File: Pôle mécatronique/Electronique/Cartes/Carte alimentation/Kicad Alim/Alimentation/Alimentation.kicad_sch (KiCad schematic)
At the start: 33 parts, among them J1 Conn_01x04, J10 24V in, J2 Conn_01x04, J3 Conn_01x04, J4 Conn_01x05, J5 Conn_01x05, J6 Conn_02x03_Odd_Even, J7 Conn_02x10_Odd_Even, J8 24V in, J9 24V out, K1 G5LE-1, Q1 BD135, SW1 SW_DPDT_x2, U1 TSR_2-2450, U2 TSR_2-2450, U3 TSR_2-24120

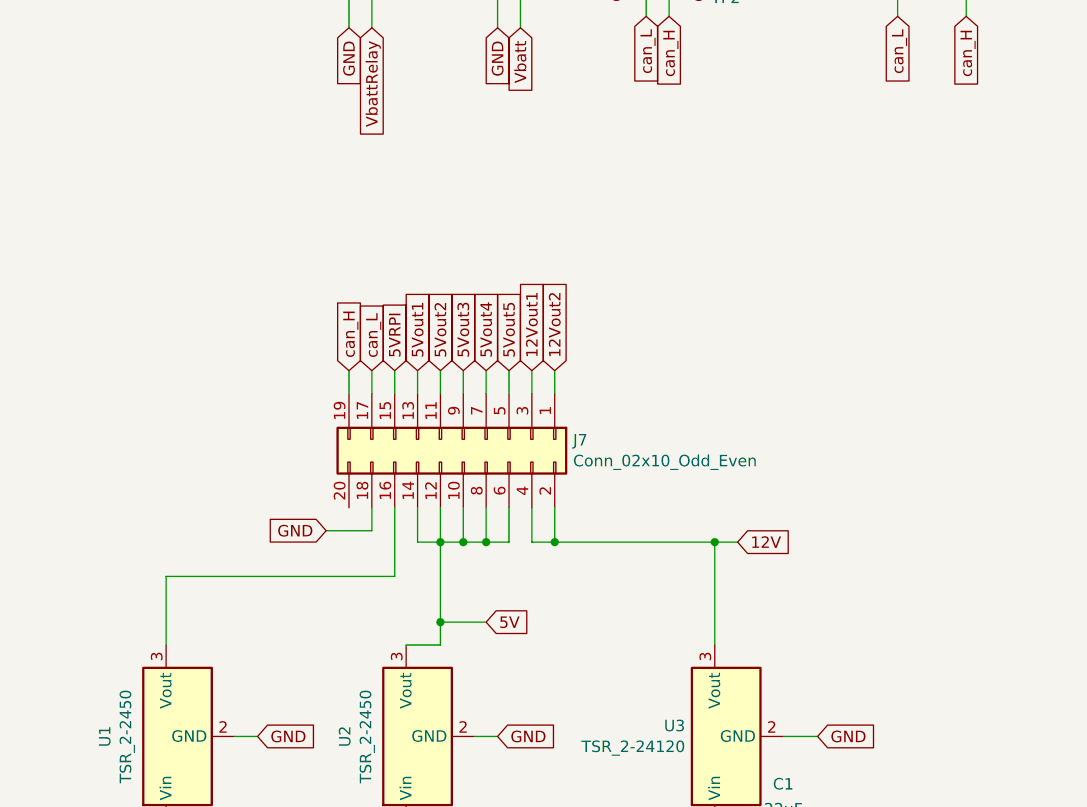
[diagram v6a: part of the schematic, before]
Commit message: Ajout points de masse
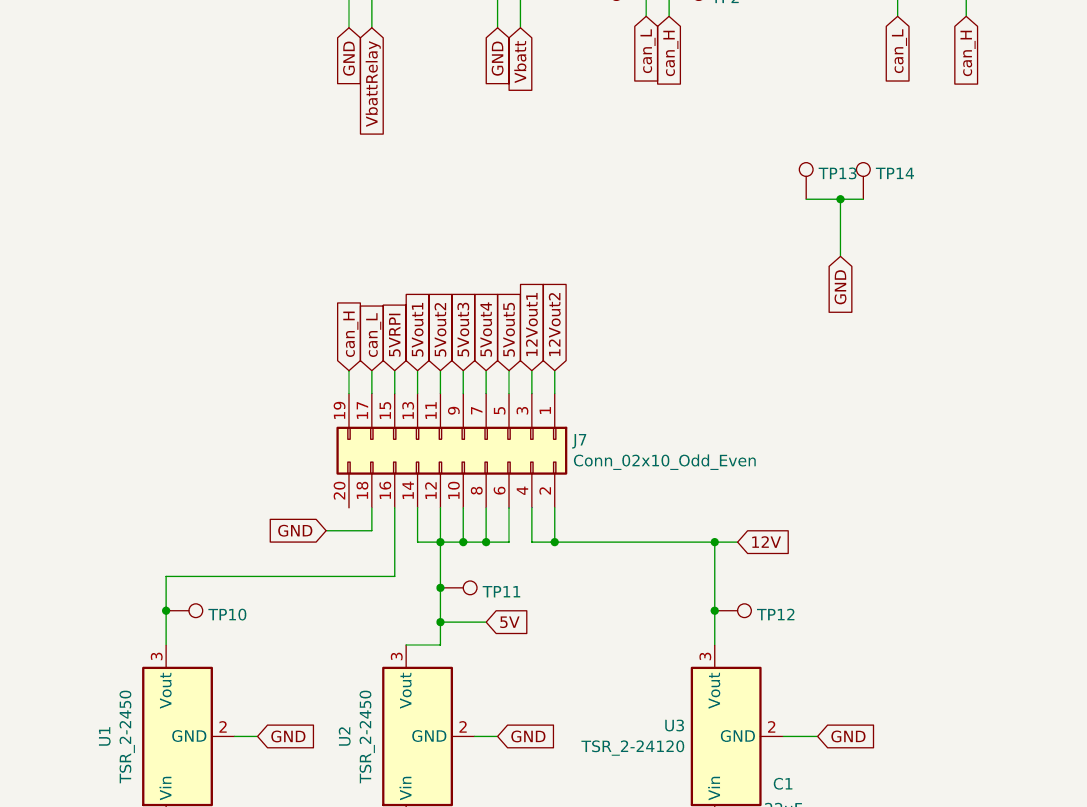
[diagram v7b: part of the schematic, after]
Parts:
- added TP10, TP11, TP12, TP13, TP14: TestPoint, TestPoint:TestPoint_Pad_D2.0mm, symbol Connector:TestPoint
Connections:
- net 12V: now also TP12.1
- net 5V: now also TP11.1
- net GND: now also TP13.1, TP14.1
- net at J7.16 (Pin_16), U1.3 (Vout): now also TP10.1
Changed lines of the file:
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@@
 (kicad_sch (version 20211123) (generator eeschema)
   (paper "A4")
+  (junction (at 63.5 140.97) (diameter 0) (color 0 0 0 0)
+  )
   (junction (at 152.4 71.12) (diameter 0) (color 0 0 0 0)
   )
@@
   (junction (at 99.06 133.35) (diameter 0) (color 0 0 0 0)
   )
+  (junction (at 138.43 95.25) (diameter 0) (color 0 0 0 0)
+  )
   (junction (at 232.41 78.74) (diameter 0) (color 0 0 0 0)
   )
@@
   (junction (at 96.52 133.35) (diameter 0) (color 0 0 0 0)
   )
+  (junction (at 124.46 140.97) (diameter 0) (color 0 0 0 0)
+  )
   (junction (at 245.11 79.8784) (diameter 0) (color 0 0 0 0)
   )
   (junction (at 93.98 133.35) (diameter 0) (color 0 0 0 0)
   )
+  (junction (at 93.98 138.43) (diameter 0) (color 0 0 0 0)
+  )
   (junction (at 232.41 76.2) (diameter 0) (color 0 0 0 0)
   )
@@
     (stroke (width 0) (type default) (color 0 0 0 0))
   )
+  (wire (pts (xy 138.43 95.25) (xy 140.97 95.25))
+    (stroke (width 0) (type default) (color 0 0 0 0))
+  )
   (wire (pts (xy 71.12 154.94) (xy 73.66 154.94))
     (stroke (width 0) (type default) (color 0 0 0 0))
@@
     (stroke (width 0) (type default) (color 0 0 0 0))
   )
+  (wire (pts (xy 124.46 140.97) (xy 124.46 133.35))
+    (stroke (width 0) (type default) (color 0 0 0 0))
+  )
   (wire (pts (xy 245.11 77.47) (xy 245.11 79.8784))
     (stroke (width 0) (type default) (color 0 0 0 0))
@@
     (stroke (width 0) (type default) (color 0 0 0 0))
   )
+  (wire (pts (xy 93.98 138.43) (xy 93.98 142.24))
+    (stroke (width 0) (type default) (color 0 0 0 0))
+  )
   (wire (pts (xy 124.46 166.37) (xy 128.27 166.37))
     (stroke (width 0) (type default) (color 0 0 0 0))
@@
     (stroke (width 0) (type default) (color 0 0 0 0))
   )
-  (wire (pts (xy 63.5 137.16) (xy 63.5 144.78))
+  (wire (pts (xy 63.5 137.16) (xy 63.5 140.97))
     (stroke (width 0) (type default) (color 0 0 0 0))
   )
@@
     (stroke (width 0) (type default) (color 0 0 0 0))
   )
-  (wire (pts (xy 124.46 144.78) (xy 124.46 133.35))
+  (wire (pts (xy 124.46 144.78) (xy 124.46 140.97))
     (stroke (width 0) (type default) (color 0 0 0 0))
   )
@@
     (stroke (width 0) (type default) (color 0 0 0 0))
   )
+  (wire (pts (xy 138.43 95.25) (xy 138.43 101.6))
+    (stroke (width 0) (type default) (color 0 0 0 0))
+  )
   (wire (pts (xy 63.5 166.37) (xy 63.5 165.1))
     (stroke (width 0) (type default) (color 0 0 0 0))
@@
     (stroke (width 0) (type default) (color 0 0 0 0))
   )
+  (wire (pts (xy 134.62 95.25) (xy 138.43 95.25))
+    (stroke (width 0) (type default) (color 0 0 0 0))
+  )
   (wire (pts (xy 245.11 79.8784) (xy 245.11 80.01))
     (stroke (width 0) (type default) (color 0 0 0 0))
   )
+  (wire (pts (xy 63.5 140.97) (xy 63.5 144.78))
+    (stroke (width 0) (type default) (color 0 0 0 0))
+  )
   (wire (pts (xy 96.52 133.35) (xy 99.06 133.35))
     (stroke (width 0) (type default) (color 0 0 0 0))
@@
     (stroke (width 0) (type default) (color 0 0 0 0))
   )
-  (wire (pts (xy 93.98 133.35) (xy 93.98 142.24))
+  (wire (pts (xy 93.98 133.35) (xy 93.98 138.43))
     (stroke (width 0) (type default) (color 0 0 0 0))
   )
@@
     (effects (font (size 1.27 1.27)) (justify right))
     (property "Intersheet References" "${INTERSHEET_REFS}" (id 0) (at 238.76 -59.69 0)
+      (effects (font (size 1.27 1.27)) hide)
+    )
+  )
+  (global_label "GND" (shape input) (at 138.43 101.6 270) (fields_autoplaced)
+    (effects (font (size 1.27 1.27)) (justify right))
+    (property "Intersheet References" "${INTERSHEET_REFS}" (id 0) (at 6.35 182.88 0)
       (effects (font (size 1.27 1.27)) hide)
     )
@@
     (pin "5")
   )
+  (symbol (lib_id "Connector:TestPoint") (at 63.5 140.97 270) (unit 1)
+    (in_bom yes) (on_board yes) (fields_autoplaced)
+    (property "Reference" "TP10" (id 0) (at 68.199 141.449 90)
+      (effects (font (size 1.27 1.27)) (justify left))
+    )
+    (property "Value" "TestPoint" (id 1) (at 68.199 142.8366 90)
+      (effects (font (size 1.27 1.27)) (justify left) hide)
+    )
+    (property "Footprint" "TestPoint:TestPoint_Pad_D2.0mm" (id 2) (at 63.5 146.05 0)
+      (effects (font (size 1.27 1.27)) hide)
+    )
+    (property "Datasheet" "~" (id 3) (at 63.5 146.05 0)
+      (effects (font (size 1.27 1.27)) hide)
+    )
+    (pin "1")
+  )
   (symbol (lib_id "Connector:TestPoint") (at 232.41 76.2 90) (unit 1)
     (in_bom yes) (on_board yes) (fields_autoplaced)
@@
     (pin "2")
   )
+  (symbol (lib_id "Connector:TestPoint") (at 124.46 140.97 270) (unit 1)
+    (in_bom yes) (on_board yes) (fields_autoplaced)
+    (property "Reference" "TP12" (id 0) (at 129.159 141.449 90)
+      (effects (font (size 1.27 1.27)) (justify left))
+    )
+    (property "Value" "TestPoint" (id 1) (at 129.159 142.8366 90)
+      (effects (font (size 1.27 1.27)) (justify left) hide)
+    )
+    (property "Footprint" "TestPoint:TestPoint_Pad_D2.0mm" (id 2) (at 124.46 146.05 0)
+      (effects (font (size 1.27 1.27)) hide)
+    )
+    (property "Datasheet" "~" (id 3) (at 124.46 146.05 0)
+      (effects (font (size 1.27 1.27)) hide)
+    )
+    (pin "1")
+  )
   (symbol (lib_id "Connector:TestPoint") (at 240.03 79.8784 90) (unit 1)
     (in_bom yes) (on_board yes) (fields_autoplaced)
@@
     )
     (property "Datasheet" "~" (id 3) (at 242.57 105.41 0)
+      (effects (font (size 1.27 1.27)) hide)
+    )
+    (pin "1")
+  )
+  (symbol (lib_id "Connector:TestPoint") (at 93.98 138.43 270) (unit 1)
+    (in_bom yes) (on_board yes) (fields_autoplaced)
+    (property "Reference" "TP11" (id 0) (at 98.679 138.909 90)
+      (effects (font (size 1.27 1.27)) (justify left))
+    )
+    (property "Value" "TestPoint" (id 1) (at 98.679 140.2966 90)
+      (effects (font (size 1.27 1.27)) (justify left) hide)
+    )
+    (property "Footprint" "TestPoint:TestPoint_Pad_D2.0mm" (id 2) (at 93.98 143.51 0)
+      (effects (font (size 1.27 1.27)) hide)
+    )
+    (property "Datasheet" "~" (id 3) (at 93.98 143.51 0)
       (effects (font (size 1.27 1.27)) hide)
     )
@@
     (pin "2")
   )
+  (symbol (lib_id "Connector:TestPoint") (at 140.97 95.25 0) (unit 1)
+    (in_bom yes) (on_board yes) (fields_autoplaced)
+    (property "Reference" "TP14" (id 0) (at 142.367 92.427 0)
+      (effects (font (size 1.27 1.27)) (justify left))
+    )
+    (property "Value" "TestPoint" (id 1) (at 142.7964 91.948 90)
+      (effects (font (size 1.27 1.27)) hide)
+    )
+    (property "Footprint" "TestPoint:TestPoint_Pad_D2.0mm" (id 2) (at 146.05 95.25 0)
+      (effects (font (size 1.27 1.27)) hide)
+    )
+    (property "Datasheet" "~" (id 3) (at 146.05 95.25 0)
+      (effects (font (size 1.27 1.27)) hide)
+    )
+    (pin "1")
+  )
   (symbol (lib_id "Device:Fuse") (at 124.46 170.18 0) (unit 1)
     (in_bom yes) (on_board yes)
@@
     )
     (property "Datasheet" "~" (id 3) (at 203.2 104.14 0)
+      (effects (font (size 1.27 1.27)) hide)
+    )
+    (pin "1")
+  )
+  (symbol (lib_id "Connector:TestPoint") (at 134.62 95.25 0) (unit 1)
+    (in_bom yes) (on_board yes) (fields_autoplaced)
+    (property "Reference" "TP13" (id 0) (at 136.017 92.427 0)
+      (effects (font (size 1.27 1.27)) (justify left))
+    )
+    (property "Value" "TestPoint" (id 1) (at 136.4464 91.948 90)
+      (effects (font (size 1.27 1.27)) hide)
+    )
+    (property "Footprint" "TestPoint:TestPoint_Pad_D2.0mm" (id 2) (at 139.7 95.25 0)
+      (effects (font (size 1.27 1.27)) hide)
+    )
+    (property "Datasheet" "~" (id 3) (at 139.7 95.25 0)
       (effects (font (size 1.27 1.27)) hide)
     )
@@
       (reference "TP9") (unit 1) (value "TestPoint") (footprint "TestPoint:TestPoint_Pad_D2.0mm")
     )
+    (path "/0574e075-2594-4438-bbc0-8c8fc583653d"
+      (reference "TP10") (unit 1) (value "TestPoint") (footprint "TestPoint:TestPoint_Pad_D2.0mm")
+    )
+    (path "/55d77ab4-691b-4b46-af02-3a8de5ec7d03"
+      (reference "TP11") (unit 1) (value "TestPoint") (footprint "TestPoint:TestPoint_Pad_D2.0mm")
+    )
+    (path "/1fcbe337-d147-4e02-846e-7f1ec4528bd0"
+      (reference "TP12") (unit 1) (value "TestPoint") (footprint "TestPoint:TestPoint_Pad_D2.0mm")
+    )
+    (path "/b8f34bd4-26e4-459e-a9ba-e24abf8e0d13"
+      (reference "TP13") (unit 1) (value "TestPoint") (footprint "TestPoint:TestPoint_Pad_D2.0mm")
+    )
+    (path "/ae8acdb7-a80f-45ac-a9ea-c3d28624f769"
+      (reference "TP14") (unit 1) (value "TestPoint") (footprint "TestPoint:TestPoint_Pad_D2.0mm")
+    )
     (path "/00000000-0000-0000-0000-000061a83da4"

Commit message: Correction Carte Alim
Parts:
- removed R3: 120, Resistor_THT:R_Axial_DIN0207_L6.3mm_D2.5mm_P10.16mm_Horizontal, symbol Device:R
- J10: value 24V in -> CAN
- R1: value 1600 -> 1k5
- R2: value 120 -> 330
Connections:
- no-connect marks 0 -> 2
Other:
- note added: "1.6k ca existe pas dans la série E12 On prendra alors 1.5k"
- note added: "mauvais nom"
- note added: "mauvaise resistance R=n*60 n étant le nombre de terminaisons soit 60*5 soit 300ohm. don on met une 330"
- note added: "sert a quoi le switch ?"
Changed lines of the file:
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@@
   (junction (at 63.5 140.97) (diameter 0) (color 0 0 0 0)
   )
-  (junction (at 152.4 71.12) (diameter 0) (color 0 0 0 0)
-  )
   (junction (at 106.68 133.35) (diameter 0) (color 0 0 0 0)
   )
@@
   (junction (at 232.41 76.2) (diameter 0) (color 0 0 0 0)
   )
-  (junction (at 144.78 71.12) (diameter 0) (color 0 0 0 0)
-  )
   (junction (at 240.03 79.8784) (diameter 0) (color 0 0 0 0)
   )
@@
   (junction (at 93.98 142.24) (diameter 0) (color 0 0 0 0)
   )
+  (no_connect (at 29.21 71.12))
+  (no_connect (at 83.82 129.54))
   (wire (pts (xy 86.36 132.08) (xy 86.36 129.54))
     (stroke (width 0) (type default) (color 0 0 0 0))
@@
     (stroke (width 0) (type default) (color 0 0 0 0))
   )
-  (wire (pts (xy 144.78 71.12) (xy 144.78 74.93))
-    (stroke (width 0) (type default) (color 0 0 0 0))
-  )
   (wire (pts (xy 85.09 30.48) (xy 85.09 33.02))
     (stroke (width 0) (type default) (color 0 0 0 0))
@@
     (stroke (width 0) (type default) (color 0 0 0 0))
   )
-  (wire (pts (xy 152.4 63.5) (xy 152.4 71.12))
+  (wire (pts (xy 152.4 63.5) (xy 152.4 74.93))
     (stroke (width 0) (type default) (color 0 0 0 0))
   )
@@
     (stroke (width 0) (type default) (color 0 0 0 0))
   )
-  (wire (pts (xy 152.4 71.12) (xy 152.4 74.93))
-    (stroke (width 0) (type default) (color 0 0 0 0))
-  )
   (wire (pts (xy 82.55 30.48) (xy 82.55 33.02))
     (stroke (width 0) (type default) (color 0 0 0 0))
@@
     (stroke (width 0) (type default) (color 0 0 0 0))
   )
-  (wire (pts (xy 144.78 63.5) (xy 144.78 71.12))
+  (wire (pts (xy 144.78 63.5) (xy 144.78 74.93))
     (stroke (width 0) (type default) (color 0 0 0 0))
   )
@@
   )
   (text "Commande relais de coupure du rail 24V" (at 199.39 54.61 0)
+    (effects (font (size 1.27 1.27)) (justify left bottom))
+  )
+  (text "1.6k ca existe pas dans la série E12\nOn prendra alors 1.5k"
+    (at 189.23 114.3 0)
+    (effects (font (size 1.27 1.27)) (justify left bottom))
+  )
+  (text "mauvaise resistance\nR=n*60\nn étant le nombre de terminaisons\nsoit 60*5 soit 300ohm. don on met une 330"
+    (at 133.35 54.61 0)
+    (effects (font (size 1.27 1.27)) (justify left bottom))
+  )
+  (text "sert a quoi le switch ?" (at 246.38 66.04 0)
+    (effects (font (size 1.27 1.27)) (justify left bottom))
+  )
+  (text "mauvais nom" (at 113.03 60.96 0)
     (effects (font (size 1.27 1.27)) (justify left bottom))
   )
@@
     (in_bom yes) (on_board yes)
     (property "Reference" "R1" (id 0) (at 213.36 98.8822 90))
-    (property "Value" "1600" (id 1) (at 213.36 101.1936 90))
+    (property "Value" "1k5" (id 1) (at 213.36 101.1936 90))
     (property "Footprint" "Resistor_THT:R_Axial_DIN0207_L6.3mm_D2.5mm_P10.16mm_Horizontal" (id 2) (at 213.36 102.362 90)
       (effects (font (size 1.27 1.27)) hide)
@@
       (effects (font (size 1.27 1.27)) (justify left))
     )
-    (property "Value" "24V in" (id 1) (at 114.808 65.7098 90)
+    (property "Value" "CAN" (id 1) (at 114.808 65.7098 90)
       (effects (font (size 1.27 1.27)) (justify left))
     )
@@
     (pin "2")
     (pin "3")
+    (pin "4")
+    (pin "5")
+    (pin "6")
   )
   (symbol (lib_id "Connector:TestPoint") (at 245.11 79.8784 270) (unit 1)
@@
     (pin "1")
   )
-  (symbol (lib_id "Device:R") (at 148.59 71.12 270) (unit 1)
-    (in_bom yes) (on_board yes)
-    (property "Reference" "R3" (id 0) (at 148.59 65.8622 90))
-    (property "Value" "120" (id 1) (at 148.59 68.1736 90))
-    (property "Footprint" "Resistor_THT:R_Axial_DIN0207_L6.3mm_D2.5mm_P10.16mm_Horizontal" (id 2) (at 148.59 69.342 90)
-      (effects (font (size 1.27 1.27)) hide)
-    )
-    (property "Datasheet" "~" (id 3) (at 148.59 71.12 0)
-      (effects (font (size 1.27 1.27)) hide)
-    )
-    (pin "1")
-    (pin "2")
-  )
   (symbol (lib_id "Connector:TestPoint") (at 140.97 95.25 0) (unit 1)
     (in_bom yes) (on_board yes) (fields_autoplaced)
@@
     (in_bom yes) (on_board yes)
     (property "Reference" "R2" (id 0) (at 148.59 58.2422 90))
-    (property "Value" "120" (id 1) (at 148.59 60.5536 90))
+    (property "Value" "330" (id 1) (at 148.59 60.5536 90))
     (property "Footprint" "Resistor_THT:R_Axial_DIN0207_L6.3mm_D2.5mm_P10.16mm_Horizontal" (id 2) (at 148.59 61.722 90)
       (effects (font (size 1.27 1.27)) hide)
@@
     )
     (path "/1e9dcbc0-ed04-41e3-9512-fbb37cd7d179"
-      (reference "J10") (unit 1) (value "24V in") (footprint "Connector_JST:JST_PH_B2B-PH-K_1x02_P2.00mm_Vertical")
+      (reference "J10") (unit 1) (value "CAN") (footprint "Connector_JST:JST_PH_B2B-PH-K_1x02_P2.00mm_Vertical")
     )
     (path "/00000000-0000-0000-0000-000061aee719"
@@
     )
     (path "/00000000-0000-0000-0000-000061b93dbb"
-      (reference "R1") (unit 1) (value "1600") (footprint "Resistor_THT:R_Axial_DIN0207_L6.3mm_D2.5mm_P10.16mm_Horizontal")
+      (reference "R1") (unit 1) (value "1k5") (footprint "Resistor_THT:R_Axial_DIN0207_L6.3mm_D2.5mm_P10.16mm_Horizontal")
     )
     (path "/c4c5a52a-59bb-4103-b05b-78908e6fcd3d"
-      (reference "R2") (unit 1) (value "120") (footprint "Resistor_THT:R_Axial_DIN0207_L6.3mm_D2.5mm_P10.16mm_Horizontal")
-    )
-    (path "/966cd2ae-4255-4a92-af40-093e3a84f37c"
-      (reference "R3") (unit 1) (value "120") (footprint "Resistor_THT:R_Axial_DIN0207_L6.3mm_D2.5mm_P10.16mm_Horizontal")
+      (reference "R2") (unit 1) (value "330") (footprint "Resistor_THT:R_Axial_DIN0207_L6.3mm_D2.5mm_P10.16mm_Horizontal")
     )
     (path "/758271bb-4e59-4adb-88bd-b1e5d6528889"
